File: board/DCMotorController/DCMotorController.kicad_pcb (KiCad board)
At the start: 4 copper layers, 89.2 x 87.2 mm, 129 parts, among them J2 Conn_01x03_Female, M1+1 Conn_01x01_Female, M1-1 Conn_01x01_Female, M1_S1 Conn_01x03_Female, M1_S2 Conn_01x03_Female, M2+1 Conn_01x01_Female, M2-1 Conn_01x01_Female, M2_S1 Conn_01x03_Female, M2_S2 Conn_01x03_Female, Q1 Q_NMOS_GDS, Q10 Q_NMOS_GDS, Q11 Q_NMOS_GDS, Q12 Q_NMOS_GDS, Q13 Q_NMOS_GDS, Q14 Q_NMOS_GDS, Q15 Q_NMOS_GDS, Q16 Q_NMOS_GDS, Q2 Q_NMOS_GDS, Q3 Q_NMOS_GDS, Q4 Q_NMOS_GDS, Q5 Q_NMOS_GDS, Q6 Q_NMOS_GDS, Q7 Q_NMOS_GDS, Q8 Q_NMOS_GDS, Q9 Q_NMOS_GDS, U1 DS18B20, U10 TPS54360DDA, U2 IR2103, U3 IR2103, U4 ESP32-WROOM-32D, U5 IR2103, U6 IR2103, U7 TPS54360DDA, U8 AMS1117-3.3, U9 DS18B20

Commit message: first version + test firmeware
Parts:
- added D20: WS2812B, LED_SMD:LED_WS2812B_PLCC4_5.0x5.0mm_P3.2mm, F.Cu at (44.0, 65.0)
- added R23: 10k, Resistor_SMD:R_0603_1608Metric, F.Cu at (83.6, 26.3)
- added R24: 10k, Resistor_SMD:R_0603_1608Metric, F.Cu at (93.7, 26.9)
- added R25: 10k, Resistor_SMD:R_0603_1608Metric, F.Cu at (104.2, 27.3)
- added R26: 10k, Resistor_SMD:R_0603_1608Metric, F.Cu at (113.9, 27.1)
- C16, C18, C37, C38: footprint Resistor_SMD:R_1206_3216Metric -> Capacitor_SMD:C_1206_3216Metric
- C19, C20, C31, C32: footprint Capacitor_SMD:C_0603_1608Metric -> Capacitor_SMD:C_1206_3216Metric
- C21, C22, C35, C36: value 39pf (33 in stock) -> 39pf
- R1, R17, R2: footprint Resistor_SMD:R_0805_2012Metric -> Resistor_SMD:R_0603_1608Metric
- R10, R3, R4, R5, R6, R7, R8, R9: value ~100ohm -> 15
- R11: value 0ohm -> 15; footprint Resistor_SMD:R_0603_1608Metric_Pad0.98x0.95mm_HandSolder -> Resistor_SMD:R_0603_1608Metric
- R12, R22, Rvoltage1, Rvoltage2, Rvoltage3, Rvoltage4: footprint Capacitor_SMD:C_0603_1608Metric -> Resistor_SMD:R_0603_1608Metric
- moved C11 61.5 mm to (79.7, 40.4)
- moved C9 61.5 mm to (79.7, 35.4)
- moved C10 61.5 mm to (69.5, 35.5)
- moved D4 61.5 mm to (74.2, 31.5)
- moved D6 61.5 mm to (83.7, 35.0)
- moved D7 61.5 mm to (83.7, 38.0)
- moved R10 61.5 mm to (83.7, 41.0)
- moved R8 61.5 mm to (83.7, 32.5)
- moved U6 61.5 mm to (74.2, 37.0)
- moved Q5 60.4 mm to (118.5, 95.0), turned to 90 degrees
- moved Q16 60.4 mm to (91.5, 41.0), turned to -90 degrees
- moved C13 59.6 mm to (79.5, 95.6)
- moved C14 59.6 mm to (79.5, 100.6)
- moved D10 59.6 mm to (83.5, 98.6)
- moved D8 59.6 mm to (74.0, 92.1)
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- renumbered J2 to GND_TX_RX1
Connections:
- Boot1 pad 1: Net-(Boot1-Pad1) -> GND
- C1 pad 1: Net-(Boot1-Pad1) -> GND
- M1_S1 pad 3: M1_S1 -> Net-(M1_S1-Pad3)
- M1_S2 pad 3: M1_S2 -> Net-(M1_S2-Pad3)
- M2_S1 pad 3: M2_S1 -> Net-(M2_S1-Pad3)
- M2_S2 pad 3: M2_S2 -> Net-(M2_S2-Pad3)
- U4 pad 13: SENSORS_ENABLE -> M1_S1
- U4 pad 14: CUSTOM_GPIO12 -> M1_S2
- U4 pad 16: PUMP_ENABLE -> M2_S1
- U4 pad 29: PLANT_CTRL_PUMP_1 -> M2_S2
- U4 pad 8: PLANT0_MOIST -> Net-(D20-Pad4)
- U8 pad 3: 5V -> VMosfet
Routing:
- net M2_A_HI: track 18.2 -> 96.9 mm
- net M1_B_HI: track 93.2 -> 14.7 mm, vias 2 -> 0
- net M1_B_LO: track 92.0 -> 17.7 mm, vias 2 -> 0
- net M2_A_LO: track 21.2 -> 86.3 mm
- net M2_S1: track 4.70 -> 64.2 mm, vias 0 -> 3
- net M2_S2: track 4.45 -> 59.5 mm, vias 0 -> 2
- net M1_S2: track 4.64 -> 56.4 mm, vias 0 -> 3
- net M1_S1: track 4.64 -> 45.3 mm, vias 0 -> 3
- net Net-(D20-Pad4): track 0.00 -> 38.4 mm, vias 0 -> 2
- net 3_3V: track 191.8 -> 218.0 mm, vias 4 -> 5
- net Net-(C14-Pad2): track 106.3 -> 84.3 mm
- net Net-(D10-Pad2): track 26.8 -> 40.6 mm
- net Net-(D7-Pad2): track 38.7 -> 26.7 mm
- net Temp: track 158.8 -> 147.9 mm
- net Net-(D6-Pad2): track 47.8 -> 38.3 mm
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
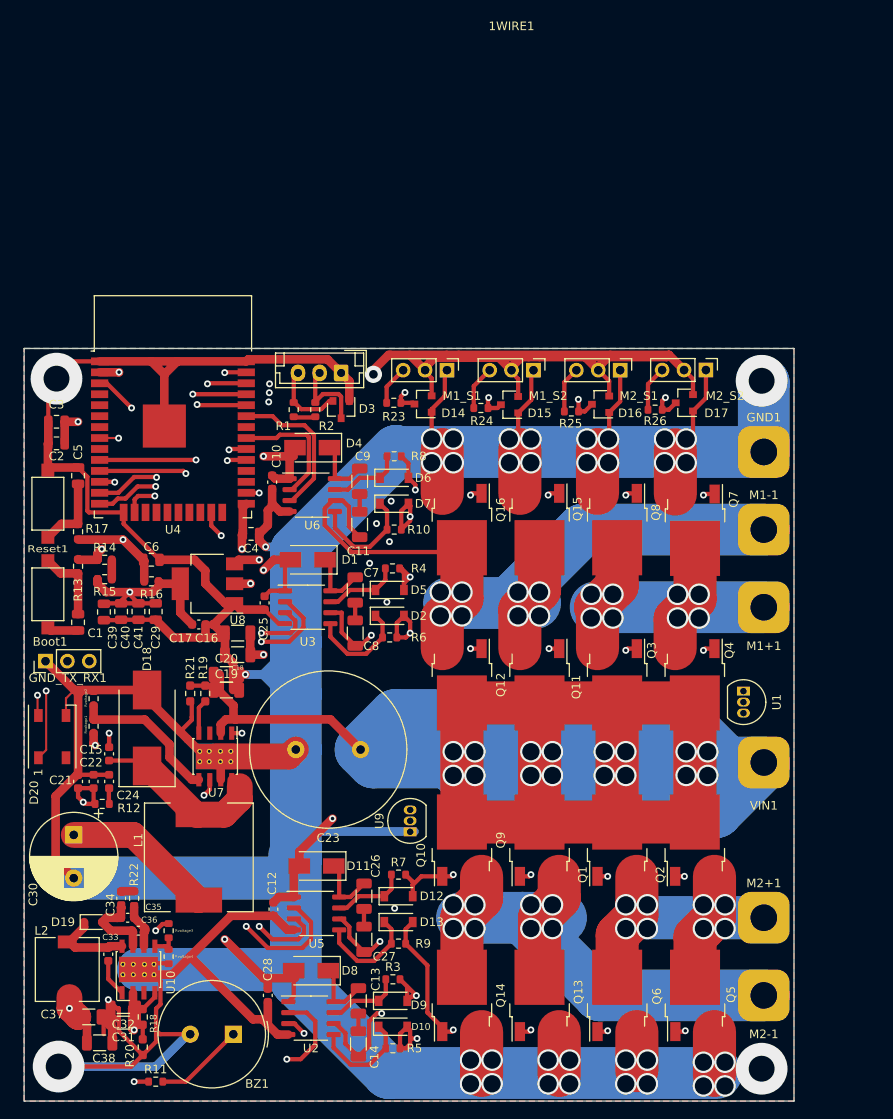
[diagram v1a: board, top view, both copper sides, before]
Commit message: Allegro current sensor edition
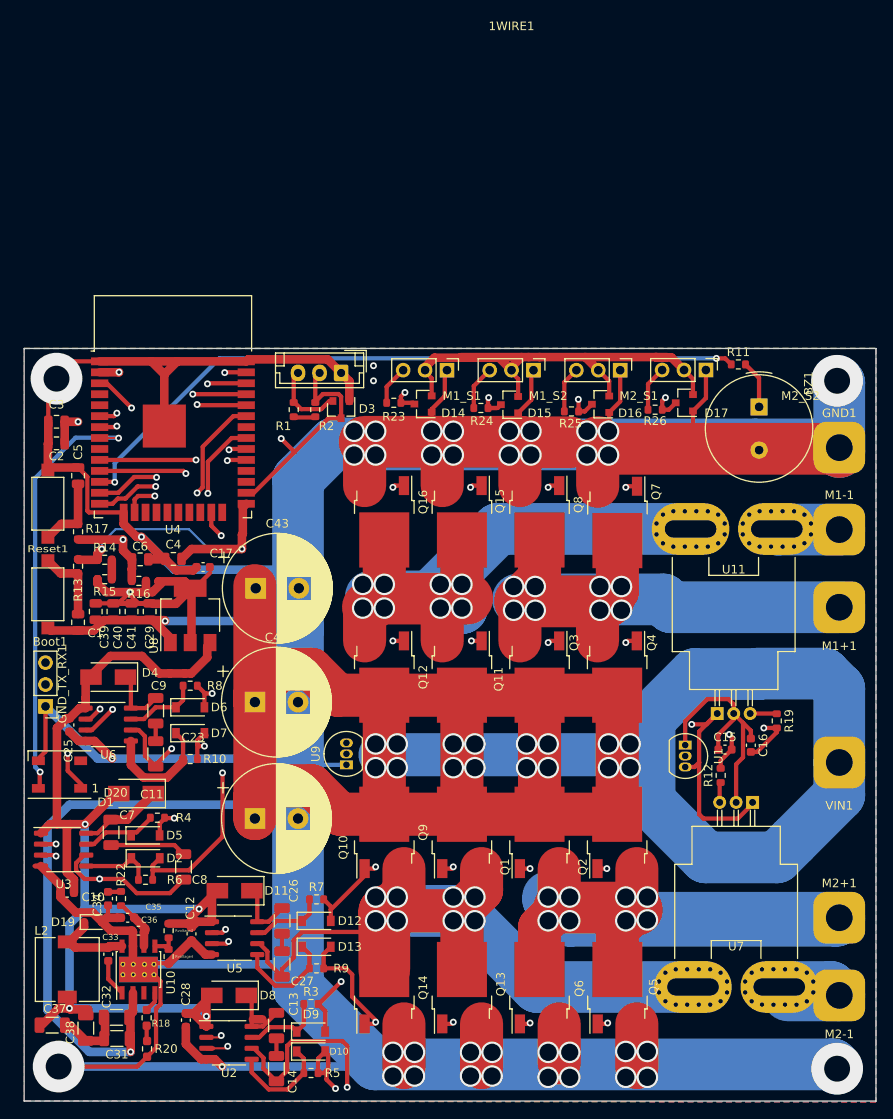
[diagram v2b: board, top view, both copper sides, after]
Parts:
- removed C18: 47uF, Capacitor_SMD:C_1206_3216Metric
- removed C19, C20: 2.2uF 60V, Capacitor_SMD:C_1206_3216Metric
- removed C21, C22: 39pf, Capacitor_SMD:C_0603_1608Metric
- removed C24: 6800pF, Capacitor_SMD:C_0603_1608Metric
- removed C30: 1000uF, Capacitor_THT:CP_Radial_D10.0mm_P5.00mm
- removed D18: B560C, Diode_SMD:D_SMC_Handsoldering
- removed L1: 8.2uH, Inductor_SMD:L_12x12mm_H8mm
- removed R21: 82k, Resistor_SMD:R_0603_1608Metric_Pad0.98x0.95mm_HandSolder
- removed Rvoltage1: 5.24*Rvoltage2 (5,6 - 7.5), Resistor_SMD:R_0603_1608Metric
- removed Rvoltage2: 1k 1.4k, Resistor_SMD:R_0603_1608Metric
- added C42: 1500uF, Capacitor_THT:CP_Radial_D12.5mm_P5.00mm, F.Cu at (67.5, 61.0)
- added C43: 1500uF, Capacitor_THT:CP_Radial_D12.5mm_P5.00mm, F.Cu at (67.6, 47.8)
- added U11: ACS758xCB-100B-PFF, Sensor_Current:Allegro_CB_PFF, F.Cu at (121.1, 62.3)
- C16: value 47uF -> 100nF; footprint Capacitor_SMD:C_1206_3216Metric -> Capacitor_SMD:C_0603_1608Metric
- C23: footprint Capacitor_THT:C_Radial_D18.0mm_H35.5mm_P7.50mm -> Capacitor_THT:CP_Radial_D12.5mm_P5.00mm
- R12: value 13k -> 1k
- R19: value 82k -> 1k; footprint Resistor_SMD:R_0603_1608Metric_Pad0.98x0.95mm_HandSolder -> Resistor_SMD:R_0603_1608Metric
- U7: value TPS54360DDA -> ACS758xCB-100B-PFF; footprint Package_SO:TI_SO-PowerPAD-8_ThermalVias -> Sensor_Current:Allegro_CB_PFF
- moved R11 107.1 mm to (123.5, 21.9)
- moved BZ1 94.9 mm to (126.0, 26.8), turned to -90 degrees
- moved R12 71.8 mm to (121.5, 69.5), turned to 90 degrees
- moved C15 71.4 mm to (122.0, 66.5), turned to 0 degrees
- moved R19 66.3 mm to (128.0, 63.2), turned to -90 degrees
- moved U7 62.5 mm to (125.2, 72.6), turned to 180 degrees
- moved C16 60.9 mm to (125.0, 66.0), turned to -90 degrees
- moved C10 53.2 mm to (45.8, 83.1), turned to 180 degrees
- moved D5 40.1 mm to (54.8, 76.5)
- moved C7 39.9 mm to (50.8, 76.1)
- moved D2 39.9 mm to (54.8, 79.1)
- moved R6 39.9 mm to (54.8, 81.6)
- moved U3 39.9 mm to (45.3, 78.1)
- moved R4 39.7 mm to (56.2, 74.4)
- moved C11 35.6 mm to (56.0, 67.0)
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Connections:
- C15 pad 1: Net-(C15-Pad1) -> GND
- C15 pad 2: Net-(C15-Pad2) -> M2_Sense
- C16 pad 1: 5V -> GND
- C16 pad 2: GND -> M1_Sense
- M1-1 pad 1: Net-(C11-Pad2) -> Net-(M1-1-Pad1)
- M2-1 pad 1: Net-(C27-Pad2) -> Net-(M2-1-Pad1)
- R12 pad 1: Net-(C21-Pad1) -> Net-(U7-Pad3)
- R12 pad 2: Net-(C24-Pad1) -> M2_Sense
- R19 pad 1: Net-(R19-Pad1) -> Net-(U11-Pad3)
- R19 pad 2: Net-(R19-Pad2) -> M1_Sense
- U4 pad 24: CUSTOM_GPIO2 -> unconnected-(U4-Pad24)
- U4 pad 4: PLANT6_MOIST -> unconnected-(U4-Pad4)
- U4 pad 5: PLANT5_MOIST -> unconnected-(U4-Pad5)
- U4 pad 6: CUSTOM_GPIO34 -> M1_Sense
- U4 pad 7: CUSTOM_GPIO35 -> M2_Sense
- U4 pad 9: PLANT1_MOIST -> unconnected-(U4-Pad9)
- U7 pad 1: Net-(C15-Pad1) -> 3_3V
- U7 pad 2: VIN -> GND
- U7 pad 3: unconnected-(U7-Pad3) -> Net-(U7-Pad3)
- U7 pad 4: Net-(R19-Pad1) -> Net-(C27-Pad2)
- U7 pad 5: Net-(Rvoltage1-Pad2) -> Net-(M2-1-Pad1)
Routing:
- net 5V: track 338.8 -> 136.9 mm, vias 4 -> 0
- net M1_Sense: track 0.00 -> 116.8 mm, vias 0 -> 3
- net M2_Sense: track 0.00 -> 110.0 mm, vias 0 -> 3
- net VIN: track 417.8 -> 341.6 mm
- net Net-(C14-Pad2): track 84.3 -> 155.7 mm
- net Net-(C8-Pad2): track 90.9 -> 160.4 mm
- net Net-(C11-Pad2): track 95.2 -> 132.6 mm, vias 8 -> 9
- net Temp: track 147.9 -> 110.8 mm
- net Net-(D2-Pad2): track 53.4 -> 90.5 mm
- net Net-(D7-Pad2): track 26.7 -> 59.9 mm
- net 3_3V: track 218.0 -> 248.1 mm
- net M1_A_LO: track 31.5 -> 61.4 mm
- net M1_B_HI: track 14.7 -> 43.9 mm, vias 0 -> 2
- net M1_B_LO: track 17.7 -> 45.7 mm, vias 0 -> 2
- net Net-(C15-Pad2): track 26.5 -> 0.00 mm
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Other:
- board size 89.2 x 87.2 mm -> 98.8 x 87.2 mm

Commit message: updated with newer 5 and 3 v supply, potentiometer supply optional added, current sensor rearangement
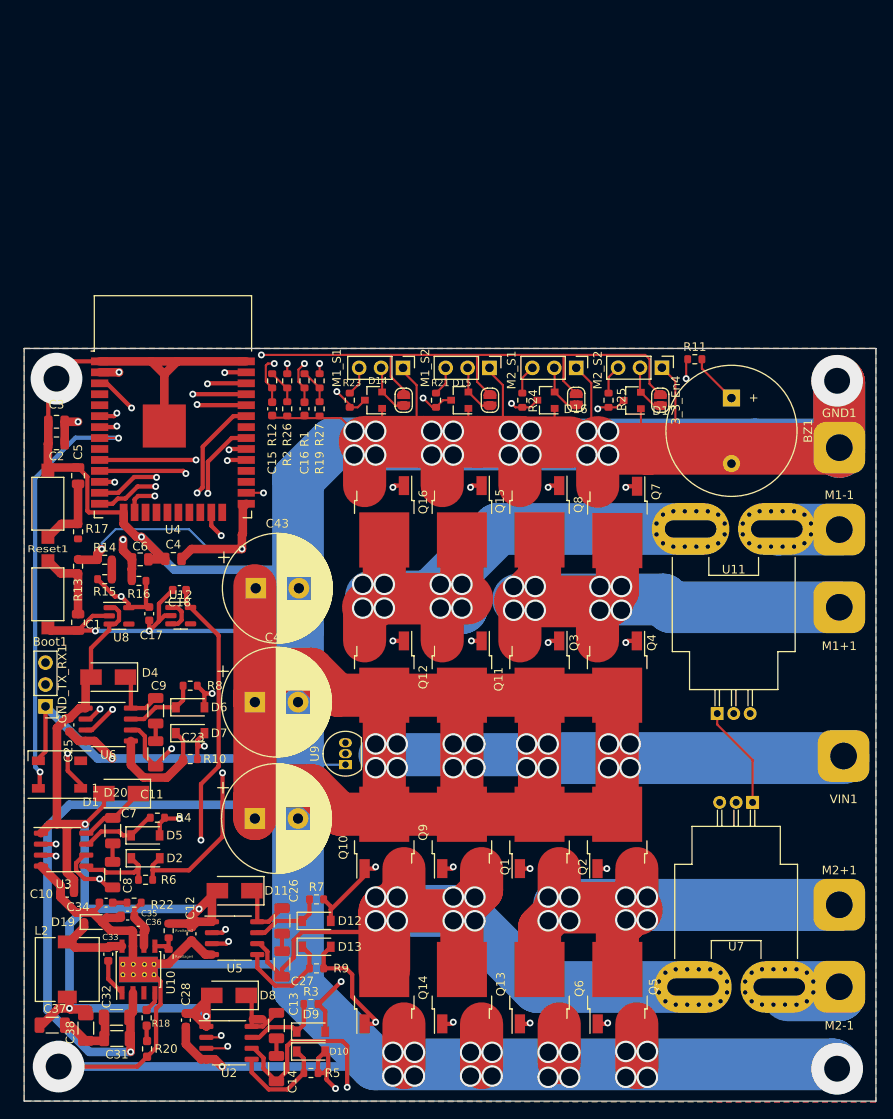
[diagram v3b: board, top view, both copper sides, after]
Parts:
- removed 1WIRE1: Conn_01x03, Connector_JST:JST_EH_B3B-EH-A_1x03_P2.50mm_Vertical
- removed C29, C39, C40, C41: 47uF, Capacitor_SMD:C_0805_2012Metric
- removed D3: BAS40-04, Package_TO_SOT_SMD:SOT-23
- removed U1: DS18B20, Package_TO_SOT_THT:TO-92_Inline
- added 3_3_En1: , Jumper:SolderJumper-2_P1.3mm_Open_RoundedPad1.0x1.5mm, F.Cu at (84.8, 26.0)
- added 3_3_En2: , Jumper:SolderJumper-2_P1.3mm_Open_RoundedPad1.0x1.5mm, F.Cu at (94.8, 26.0)
- added 3_3_En3: , Jumper:SolderJumper-2_P1.3mm_Open_RoundedPad1.0x1.5mm, F.Cu at (104.8, 25.9)
- added 3_3_En4: , Jumper:SolderJumper-2_P1.3mm_Open_RoundedPad1.0x1.5mm, F.Cu at (114.5, 26.0)
- added C18: 22uF, Capacitor_SMD:C_0603_1608Metric, F.Cu at (58.8, 48.0)
- added R21: 10k, Resistor_SMD:R_0603_1608Metric, F.Cu at (88.5, 26.0)
- added R27: 2k7, Resistor_SMD:R_0603_1608Metric, F.Cu at (75.0, 23.8)
- added U12: SPX3819M5-L-5-0, Package_TO_SOT_SMD:SOT-23-5, F.Cu at (58.9, 51.0)
- BZ1: footprint Buzzer_Beeper:Buzzer_TDK_PS1240P02BT_D12.2mm_H6.5mm -> Buzzer_Beeper:Buzzer_15x7.5RM7.6
- R19, R2: value 1k -> 2k7
- R26: value 10k -> 2k7
- U8: value AMS1117-3.3 -> SPX3819M5-L-3-3; footprint Package_TO_SOT_SMD:SOT-223-3_TabPin2 -> Package_TO_SOT_SMD:SOT-23-5
- moved R12 69.3 mm to (69.5, 23.8), turned to -90 degrees
- moved C15 65.7 mm to (69.5, 27.0), turned to -90 degrees
- moved C16 64.8 mm to (73.2, 27.0)
- moved R19 64.2 mm to (75.0, 27.0), turned to 90 degrees
- moved R26 42.8 mm to (71.2, 23.8), turned to 90 degrees
- moved C8 8.27 mm to (51.0, 81.0)
- moved C17 8.26 mm to (55.2, 50.8), turned to -90 degrees
- moved U8 8.25 mm to (51.8, 51.0), turned to 0 degrees
- moved D16 6.34 mm to (101.2, 26.0)
- moved D17 6.05 mm to (111.2, 26.0)
- moved D15 5.79 mm to (91.2, 26.0)
- moved D14 5.76 mm to (81.2, 26.0)
- moved R23 5.11 mm to (78.5, 26.0), turned to -90 degrees
- moved M1_S2 5.11 mm to (94.7, 22.2)
- moved M2_S2 5.11 mm to (114.7, 22.2)
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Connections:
- C15 pad 1: GND -> M2_Sense
- C15 pad 2: M2_Sense -> GND
- C16 pad 1: GND -> M1_Sense
- C16 pad 2: M1_Sense -> GND
- D14 pad 2: 5V -> Net-(D14-Pad2)
- D15 pad 2: 5V -> Net-(M1_S2-Pad2)
- D16 pad 2: 5V -> Net-(M2_S1-Pad2)
- D17 pad 2: 5V -> Net-(M2_S2-Pad2)
- M1_S1 pad 2: 5V -> Net-(D14-Pad2)
- M1_S2 pad 2: 5V -> Net-(M1_S2-Pad2)
- M2_S1 pad 2: 5V -> Net-(M2_S1-Pad2)
- M2_S2 pad 2: 5V -> Net-(M2_S2-Pad2)
- R1 pad 2: 3_3V -> M1_Sense
- R12 pad 1: Net-(U7-Pad3) -> Net-(R12-Pad1)
- R19 pad 1: Net-(U11-Pad3) -> GND
- R19 pad 2: M1_Sense -> Net-(R1-Pad1)
- R2 pad 1: Net-(R1-Pad1) -> GND
- R2 pad 2: Temp -> Net-(R12-Pad1)
- R24 pad 1: Net-(M1_S2-Pad3) -> Net-(M2_S1-Pad3)
- R24 pad 2: M1_S2 -> M2_S1
- R25 pad 1: Net-(M2_S1-Pad3) -> Net-(M2_S2-Pad3)
- R25 pad 2: M2_S1 -> M2_S2
- R26 pad 1: Net-(M2_S2-Pad3) -> Net-(R12-Pad1)
- R26 pad 2: M2_S2 -> Net-(U7-Pad3)
- U11 pad 1: 3_3V -> 5V
- U4 pad 27: SCL -> unconnected-(U4-Pad27)
- U4 pad 28: SDA -> unconnected-(U4-Pad28)
- U7 pad 1: 3_3V -> 5V
- U8 pad 1: GND -> VMosfet
- U8 pad 2: 3_3V -> GND
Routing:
- net Net-(U7-Pad3): track 2.35 -> 91.5 mm, vias 0 -> 1
- net M1_Sense: track 116.8 -> 32.1 mm, vias 3 -> 2
- net M2_Sense: track 110.0 -> 29.8 mm, vias 3 -> 2
- net Net-(U11-Pad3): track 3.09 -> 79.0 mm, vias 0 -> 1
- net Temp: track 110.8 -> 38.0 mm
- net 3_3V: track 248.1 -> 205.8 mm
- net VIN: track 341.6 -> 302.5 mm
- net 5V: track 136.9 -> 110.5 mm, vias 0 -> 1
- net GND: track 736.9 -> 716.1 mm, vias 40 -> 41
- net Net-(C8-Pad2): track 160.4 -> 145.6 mm
- net Net-(C14-Pad2): track 155.7 -> 144.0 mm
- net M2_S1: track 63.9 -> 54.1 mm
- net M1_S2: track 55.4 -> 46.6 mm
- net M2_S2: track 59.5 -> 51.1 mm
- net Net-(D5-Pad2): track 75.1 -> 67.0 mm
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
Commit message: update to newer current sensoring
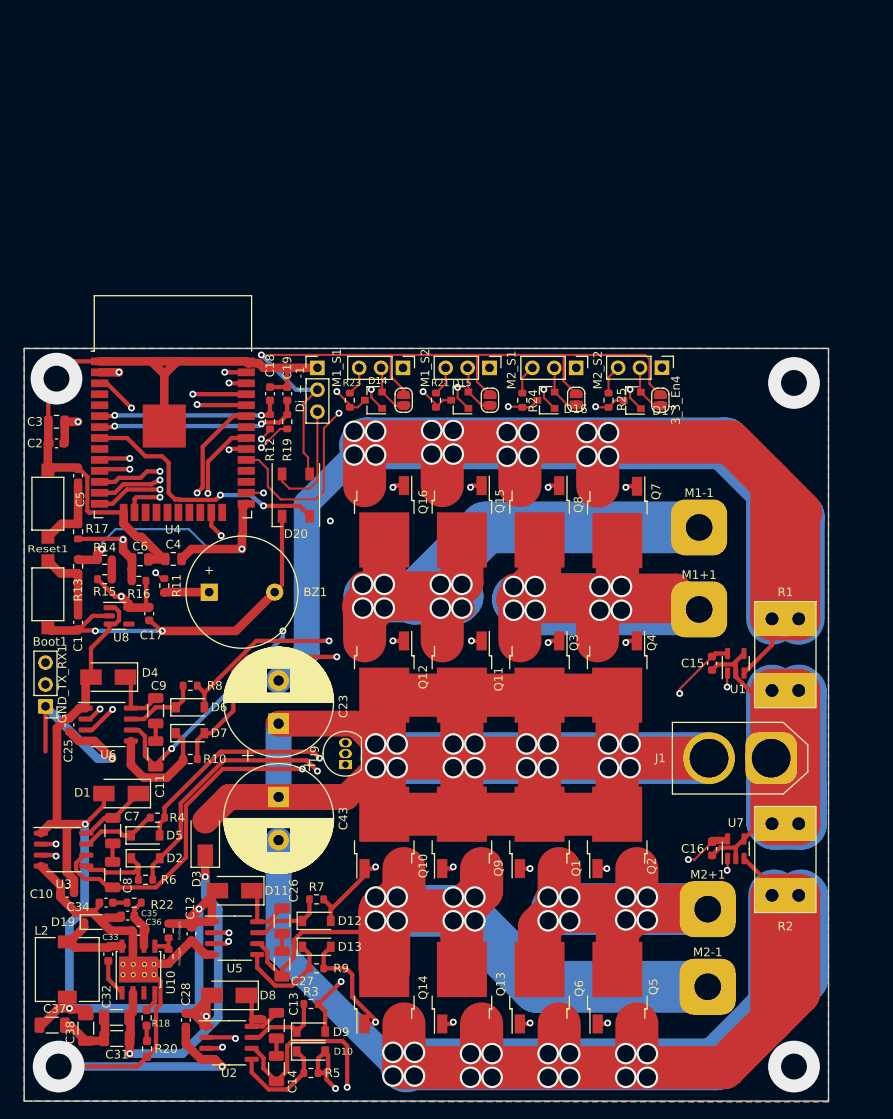
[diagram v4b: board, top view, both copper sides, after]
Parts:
- removed C42: 1500uF, Capacitor_THT:CP_Radial_D12.5mm_P5.00mm
- removed GND1, VIN1: Conn_01x01_Female, Wire-Solder:60A_Wire_solder
- removed R26, R27: 2k7, Resistor_SMD:R_0603_1608Metric
- removed U11: ACS758xCB-100B-PFF, Sensor_Current:Allegro_CB_PFF
- removed U12: SPX3819M5-L-5-0, Package_TO_SOT_SMD:SOT-23-5
- added C19: 100nF, Capacitor_SMD:C_0603_1608Metric, F.Cu at (71.2, 25.2)
- added D3: US1A, Diode_SMD:D_SMA, F.Cu at (61.8, 76.8)
- added Di_+_-1: Conn_01x03_Female, Connector_PinHeader_2.54mm:PinHeader_1x03_P2.54mm_Vertical, F.Cu at (74.8, 22.2)
- added J1: Conn_01x02, Connector_AMASS:AMASS_XT60-M_1x02_P7.20mm_Vertical, F.Cu at (127.3, 67.5)
- added U1: INA180A1, Package_TO_SOT_SMD:SOT-23-5, F.Cu at (123.2, 56.5)
- BZ1: footprint Buzzer_Beeper:Buzzer_15x7.5RM7.6 -> Wire-Solder:Buzzer_12x7.5
- C1, C2, C5: footprint Capacitor_SMD:C_0805_2012Metric -> Capacitor_SMD:C_0603_1608Metric
- C18: value 22uF -> 100nF
- C23, C43: value 1500uF -> 750uF
- R1: value 1k -> R_Shunt; footprint Resistor_SMD:R_0603_1608Metric -> Wire-Solder:Shunt 1moh 5W
- R12: value 1k -> 10k
- R19: value 2k7 -> 10k
- R2: value 2k7 -> R_Shunt; footprint Resistor_SMD:R_0603_1608Metric -> Wire-Solder:Shunt 1moh 5W
- U7: value ACS758xCB-100B-PFF -> INA180A1; footprint Sensor_Current:Allegro_CB_PFF -> Package_TO_SOT_SMD:SOT-23-5
- moved R2 79.6 mm to (127.5, 83.4)
- moved C16 69.5 mm to (120.5, 78.0)
- moved R11 66.9 mm to (57.0, 47.5), turned to -90 degrees
- moved BZ1 64.6 mm to (62.2, 48.2), turned to 0 degrees
- moved R1 63.6 mm to (130.6, 51.4)
- moved C15 58.9 mm to (120.5, 56.5)
- moved D20 42.4 mm to (72.2, 37.0), turned to -90 degrees
- moved C18 25.1 mm to (69.2, 25.2), turned to -90 degrees
- moved C43 24.3 mm to (70.2, 72.0), turned to -90 degrees
- moved M1+1 16.3 mm to (119.0, 50.2)
- moved M1-1 16.3 mm to (119.0, 40.8)
- moved M2+1 15.3 mm to (120.0, 85.0)
- moved M2-1 15.2 mm to (120.0, 94.0)
- moved C23 11.3 mm to (70.2, 63.5), turned to 90 degrees
- moved U7 5.72 mm to (123.2, 78.0), turned to 90 degrees
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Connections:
- C15 pad 1: M2_Sense -> 3_3V
- C16 pad 1: M1_Sense -> 3_3V
- C18 pad 1: 5V -> GND
- C18 pad 2: GND -> M1_Sense
- C23 pad 2: GND -> M1_Shunt
- C31 pad 1: VIN -> Net-(C31-Pad1)
- C32 pad 1: VIN -> Net-(C31-Pad1)
- C43 pad 2: GND -> M2_Shunt
- D20 pad 2: unconnected-(D20-Pad2) -> Net-(D20-Pad2)
- M1-1 pad 1: Net-(M1-1-Pad1) -> Net-(C11-Pad2)
- M2-1 pad 1: Net-(U7-Pad5) -> Net-(C27-Pad2)
- Q13 pad 3: GND -> M2_Shunt
- Q14 pad 3: GND -> M2_Shunt
- Q15 pad 3: GND -> M1_Shunt
- Q16 pad 3: GND -> M1_Shunt
- Q5 pad 3: GND -> M2_Shunt
- Q6 pad 3: GND -> M2_Shunt
- Q7 pad 3: GND -> M1_Shunt
- Q8 pad 3: GND -> M1_Shunt
- R1 pad 1: Net-(R1-Pad1) -> M1_Shunt
- R1 pad 2: M1_Sense -> GND
- R12 pad 1: Net-(R12-Pad1) -> M1_Sense
- R12 pad 2: M2_Sense -> Net-(R12-Pad2)
- R19 pad 1: GND -> M2_Sense
- R19 pad 2: Net-(R1-Pad1) -> Net-(R19-Pad2)
- R2 pad 1: GND -> M2_Shunt
- R2 pad 2: Net-(R12-Pad1) -> GND
- U10 pad 2: VIN -> Net-(C31-Pad1)
- U7 pad 1: 5V -> Net-(R19-Pad2)
- U7 pad 3: Net-(U7-Pad3) -> M2_Shunt
- U7 pad 4: Net-(C27-Pad2) -> GND
- U7 pad 5: Net-(U7-Pad5) -> 3_3V
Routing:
- net M1_Shunt: track 0.00 -> 226.1 mm, vias 0 -> 16
- net M2_Shunt: track 0.00 -> 210.9 mm, vias 0 -> 16
- net 5V: track 110.5 -> 0.00 mm, vias 1 -> 0
- net Net-(R19-Pad2): track 0.00 -> 102.7 mm, vias 0 -> 2
- net Net-(U7-Pad3): track 91.5 -> 0.00 mm, vias 1 -> 0
- net Net-(R12-Pad2): track 0.00 -> 83.2 mm, vias 0 -> 2
- net Net-(U11-Pad3): track 79.0 -> 0.00 mm, vias 1 -> 0
- net VIN: track 302.5 -> 227.4 mm, vias 17 -> 16
- net GND: track 716.1 -> 643.9 mm, vias 41 -> 12
- net 3_3V: track 205.8 -> 270.7 mm, vias 5 -> 7
- net Net-(R11-Pad1): track 78.1 -> 21.0 mm
- net Net-(C31-Pad1): track 0.00 -> 38.2 mm, vias 0 -> 2
- net Net-(C8-Pad2): track 145.6 -> 176.2 mm
- net Net-(D20-Pad4): track 49.7 -> 30.5 mm
- net Net-(D20-Pad2): track 0.00 -> 13.7 mm
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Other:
- board size 98.8 x 87.2 mm -> 93.2 x 87.2 mm
